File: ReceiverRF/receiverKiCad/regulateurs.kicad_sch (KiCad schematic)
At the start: 15 parts, among them SW5 SW_SPST, U2 NCV5501DT33RKG, U3 NJM2882F05-TE1

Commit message: changement vers footprint 1206
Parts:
- PWR_C2, PWR_C3: footprint Capacitor_SMD:C_0603_1608Metric -> Capacitor_SMD:C_1206_3216Metric
- PWR_C4, PWR_C5: footprint Capacitor_SMD:C_0402_1005Metric -> Capacitor_SMD:C_1206_3216Metric
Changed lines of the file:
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@@
 			)
 		)
-		(property "Footprint" "Capacitor_SMD:C_0603_1608Metric"
+		(property "Footprint" "Capacitor_SMD:C_1206_3216Metric"
 			(at 202.8952 90.17 0)
 			(effects
@@
 			)
 		)
-		(property "Footprint" "Capacitor_SMD:C_0603_1608Metric"
+		(property "Footprint" "Capacitor_SMD:C_1206_3216Metric"
 			(at 64.4652 77.47 0)
 			(effects
@@
 			)
 		)
-		(property "Footprint" "Capacitor_SMD:C_0402_1005Metric"
+		(property "Footprint" "Capacitor_SMD:C_1206_3216Metric"
 			(at 191.4652 100.33 0)
 			(effects
@@
 			)
 		)
-		(property "Footprint" "Capacitor_SMD:C_0402_1005Metric"
+		(property "Footprint" "Capacitor_SMD:C_1206_3216Metric"
 			(at 121.6152 97.79 0)
 			(effects

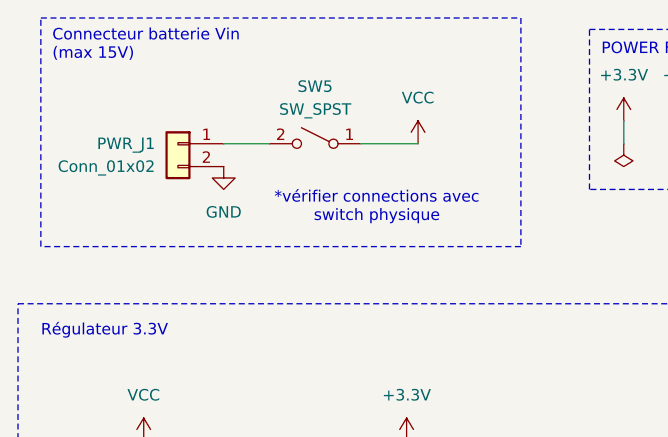
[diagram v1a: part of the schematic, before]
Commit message: changement BOM et choix nouvelles pièces 1206
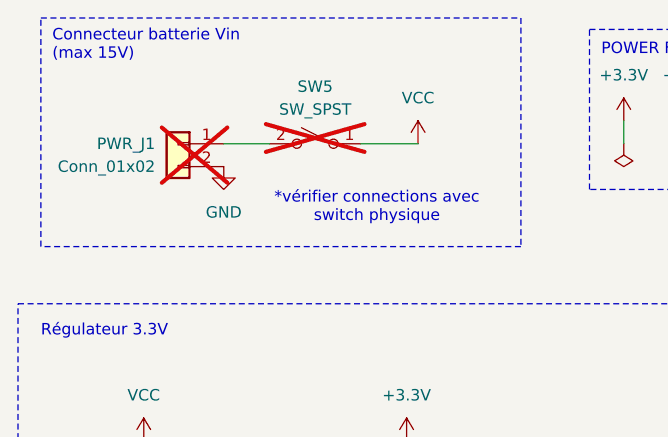
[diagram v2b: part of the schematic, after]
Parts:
- PWR_C2: Digikey 4713-GMC10X7R475K10NTCT-ND -> 1276-3182-1-ND
- PWR_C3: Digikey 2679-AGC0603X7R250-105KXPTR-ND -> 1276-1068-1-ND
- PWR_C4: Digikey 2679-AGC0402X7R500-104KNPTR-ND -> 399-C1206C104K5RACTUCT-ND
- PWR_C5: Digikey 2679-AGC0402X7R500-103KNPTR-ND -> 311-1174-1-ND
- PWR_J1, SW5: now not fitted
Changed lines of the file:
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@@
 			)
 		)
-		(property "Digikey" "  2679-AGC0603X7R250-105KXPTR-ND"
+		(property "Digikey" "1276-1068-1-ND"
 			(at 201.93 86.36 0)
 			(effects
@@
 		(in_bom yes)
 		(on_board yes)
-		(dnp no)
+		(dnp yes)
 		(property "Reference" "SW5"
 			(at 53.34 26.67 0)
@@
 			)
 		)
-		(property "Digikey" "4713-GMC10X7R475K10NTCT-ND"
+		(property "Digikey" "1276-3182-1-ND"
 			(at 63.5 73.66 0)
 			(effects
@@
 			)
 		)
-		(property "Digikey" "  2679-AGC0402X7R500-103KNPTR-ND"
+		(property "Digikey" "311-1174-1-ND"
 			(at 190.5 96.52 0)
 			(effects
@@
 		(in_bom yes)
 		(on_board yes)
-		(dnp no)
+		(dnp yes)
 		(property "Reference" "PWR_J1"
 			(at 35.56 33.02 0)
@@
 			)
 		)
-		(property "Digikey" "2679-AGC0402X7R500-104KNPTR-ND"
+		(property "Digikey" "399-C1206C104K5RACTUCT-ND"
 			(at 120.65 93.98 0)
 			(effects

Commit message: ideFIX v2 fix schematic, layout
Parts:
- removed SW5: SW_SPST, Footprints:SW_1MS02Q_CNK, symbol Switch:SW_SPST
- added D1: BZV55C18, Diode_SMD:D_MiniMELF, symbol Diode:BZV55C18
- added PWR_R5: 100k, Resistor_SMD:R_1206_3216Metric, symbol Device:R
- added Q2: PMOS, Footprints:SOT-23, symbol Simulation_SPICE:PMOS
- added SW5: SW_SPDT, Footprints:CS12ANW03_NKK, symbol Switch:SW_SPDT
- PWR_J1: footprint Connector_PinHeader_2.00mm:PinHeader_1x02_P2.00mm_Vertical -> Connector_PinHeader_2.54mm:PinHeader_1x02_P2.54mm_Vertical; now fitted
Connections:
- net GND: now also PWR_R5.2
- net VCC: now also D1.1 (K), Q2.3 (S)
- net at PWR_J1.1 (Pin_1): now also SW5.2 (B)
- new net: D1.2 (A), PWR_R5.1, Q2.2 (G)
- new net: Q2.1 (D), SW5.1 (A)
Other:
- note added: "Connecteur batterie Vin (max 20V)"
- note added: "Protection polarité inverse"
- note removed: "Connecteur batterie Vin (max 15V)"
- moved on the sheet: PWR_C1, PWR_C2, PWR_C3, PWR_C4, PWR_C5, PWR_D1, PWR_D2, PWR_R1, PWR_R2, PWR_R3, PWR_R4, U2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

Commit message: revision schematic before tracing
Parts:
- D1: value BZV55C18 -> SZMMSZ4679T1G
- PWR_R5: Digikey (none) -> 541-100KUTR-ND
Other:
- company: (none) -> GAUL
- title: (none) -> IdeFIX
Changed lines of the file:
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@@
 	(generator_version "8.0")
 	(paper "A4")
+	(title_block
+		(title "IdeFIX")
+		(rev "v2")
+		(company "GAUL")
+	)
 	(junction
 		(at 71.12 45.72)
@@
 			)
 		)
-		(property "Value" "BZV55C18"
+		(property "Value" "SZMMSZ4679T1G"
 			(at 81.28 41.9099 90)
 			(effects
@@
 			)
 		)
-		(property "Datasheet" "https://assets.nexperia.com/documents/data-sheet/BZV55_SER.pdf"
+		(property "Datasheet" "https://www.digikey.ca/en/products/detail/onsemi/SZMMSZ4679T1G/5404986?s=N4IgTCBcDaIMoC0CyTEBYBsB2AnAFQEYBxAeTgGE8BaAOQBEQBdAXyA"
 			(at 78.74 40.64 0)
 			(effects
@@
 			)
 		)
-		(property "Datasheet" "https://ngspice.sourceforge.io/docs/ngspice-html-manual/manual.xhtml#cha_MOSFETs"
+		(property "Datasheet" "https://www.digikey.ca/en/products/detail/onsemi/NTR4101PT1G/687096?s=N4IgTCBcDaIHIBUBKAWAjABjQBQWg4gPIDKAwggLRwAiIAugL5A"
 			(at 83.82 38.1 0)
 			(effects
@@
 			)
 		)
-		(property "Datasheet" "~"
+		(property "Datasheet" "https://www.digikey.ca/en/products/detail/vishay-dale/CRCW1206100KFKEAHP/2222454"
 			(at 71.12 50.8 0)
 			(effects
@@
 			)
 		)
-		(property "Digikey" ""
+		(property "Digikey" "  541-100KUTR-ND"
 			(at 71.12 50.8 0)
 			(effects

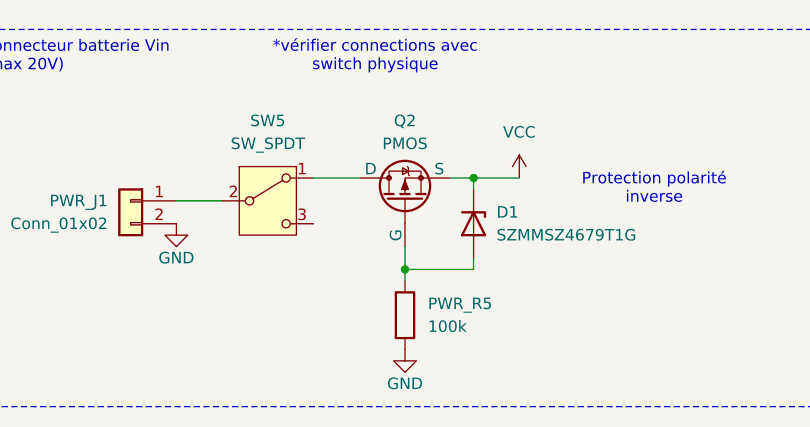
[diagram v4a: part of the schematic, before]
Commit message: finished silkscreen and added logos
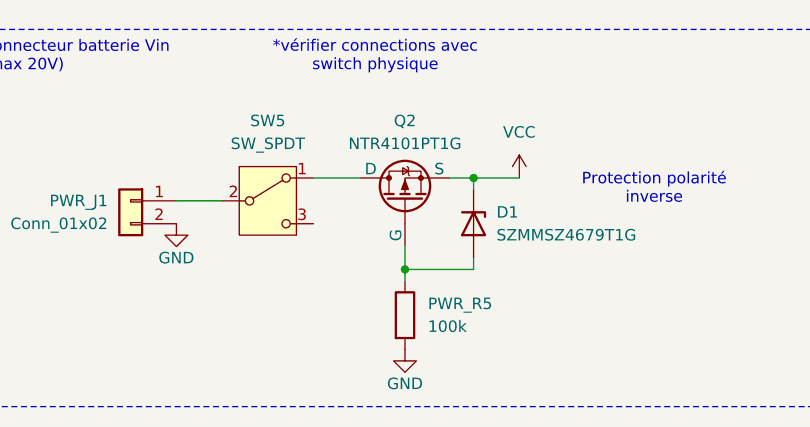
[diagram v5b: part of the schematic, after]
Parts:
- Q2: value PMOS -> NTR4101PT1G
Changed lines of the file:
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@@
 			)
 		)
-		(property "Value" "PMOS"
+		(property "Value" "NTR4101PT1G"
 			(at 71.12 31.75 90)
 			(effects

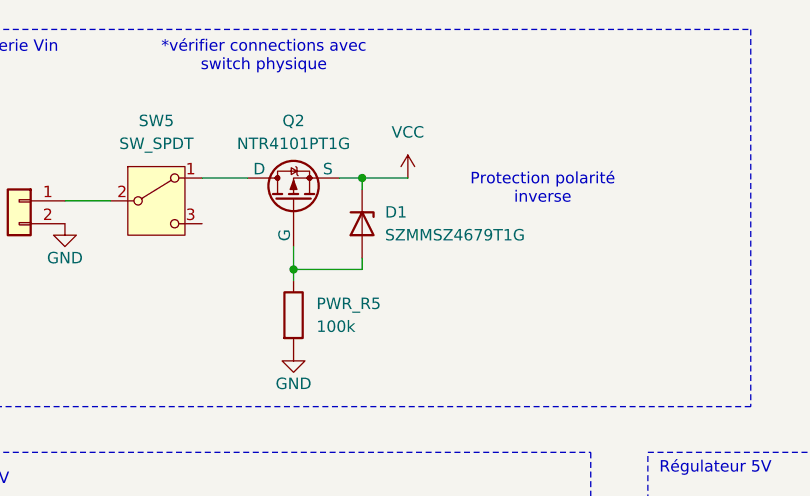
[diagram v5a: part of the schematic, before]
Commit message: fix zener diode footprint, thermal relief on SMA conn, more work on silkscreen
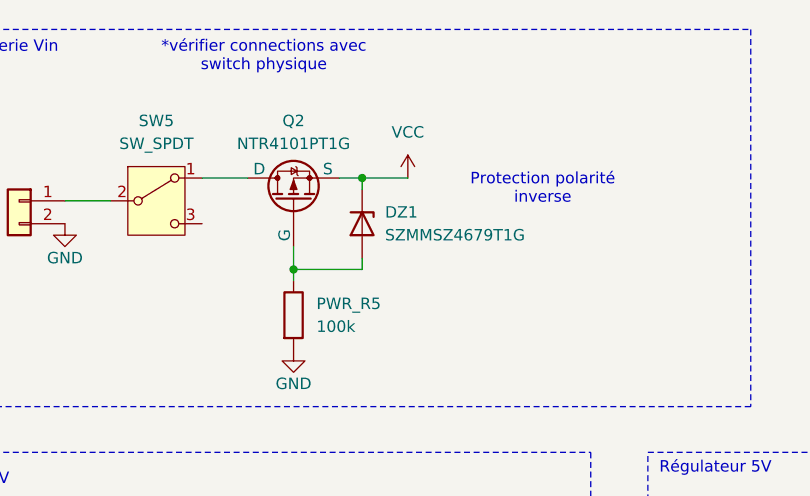
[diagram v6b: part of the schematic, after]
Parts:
- DZ1: renamed from D1; footprint Diode_SMD:D_MiniMELF -> Diode_SMD:D_SOD-123
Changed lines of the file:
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@@
 		(dnp no)
 		(fields_autoplaced yes)
-		(property "Reference" "D1"
+		(property "Reference" "DZ1"
 			(at 81.28 39.3699 90)
 			(effects
@@
 			)
 		)
-		(property "Footprint" "Diode_SMD:D_MiniMELF"
+		(property "Footprint" "Diode_SMD:D_SOD-123"
 			(at 74.295 40.64 0)
 			(effects
@@
 			(project ""
 				(path "/439ba515-58d4-4b14-87ab-b438dcf423a5/daa1b3d3-1e11-4b02-868f-dd095818f20a"
-					(reference "D1")
+					(reference "DZ1")
 					(unit 1)
 				)

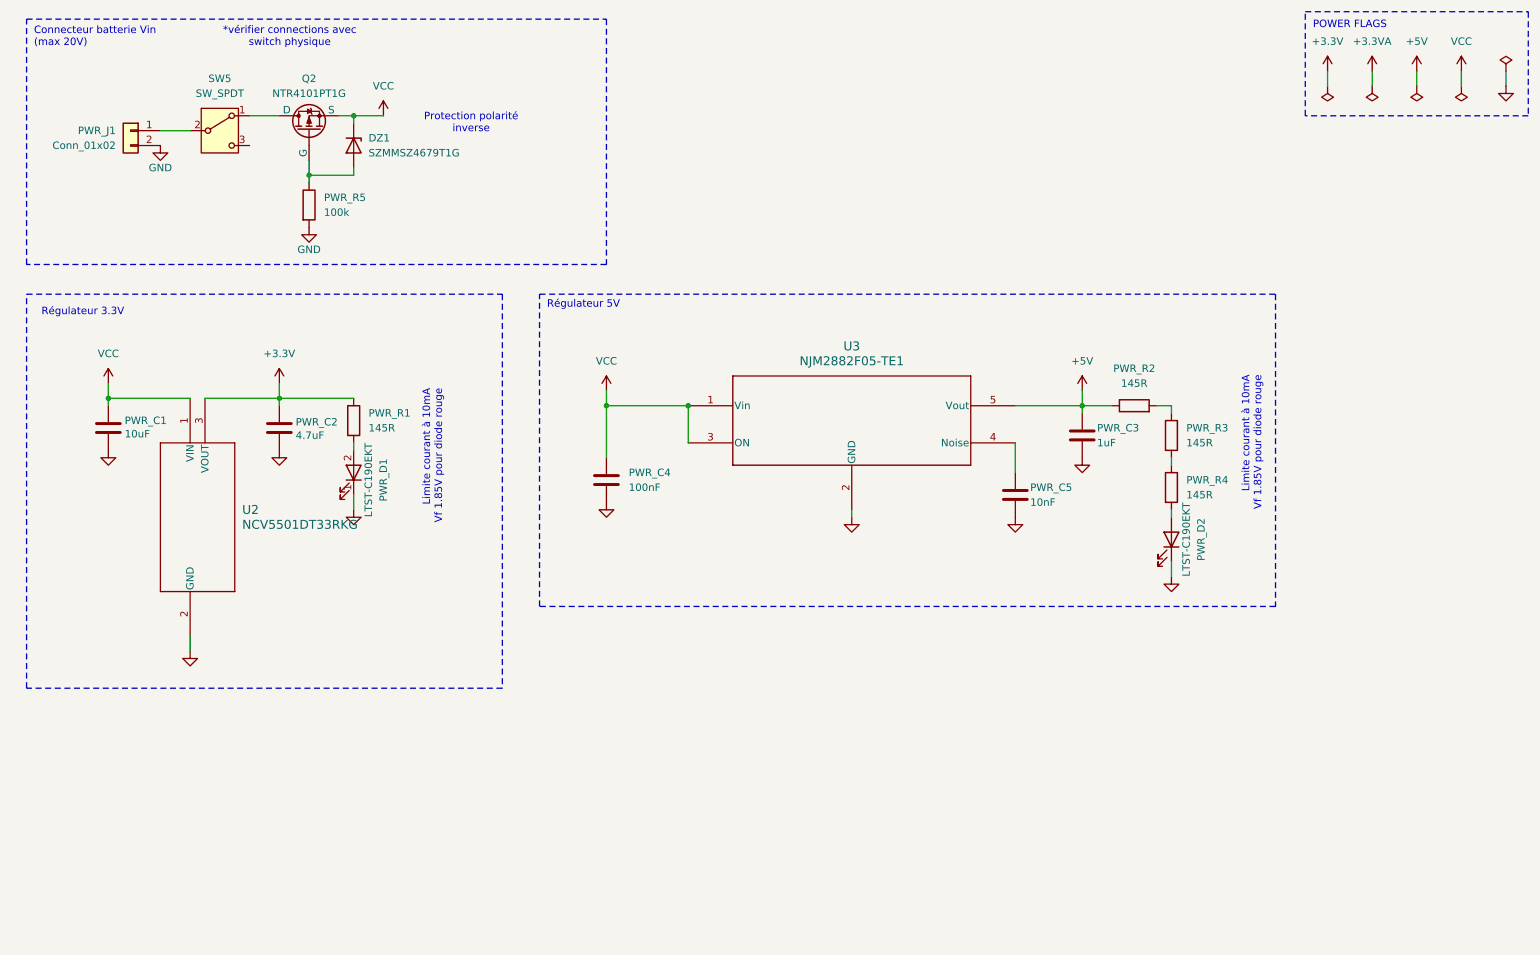
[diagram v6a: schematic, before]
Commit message: 3.2mm holes, XT30 connector, add polyfuse, minor fixes
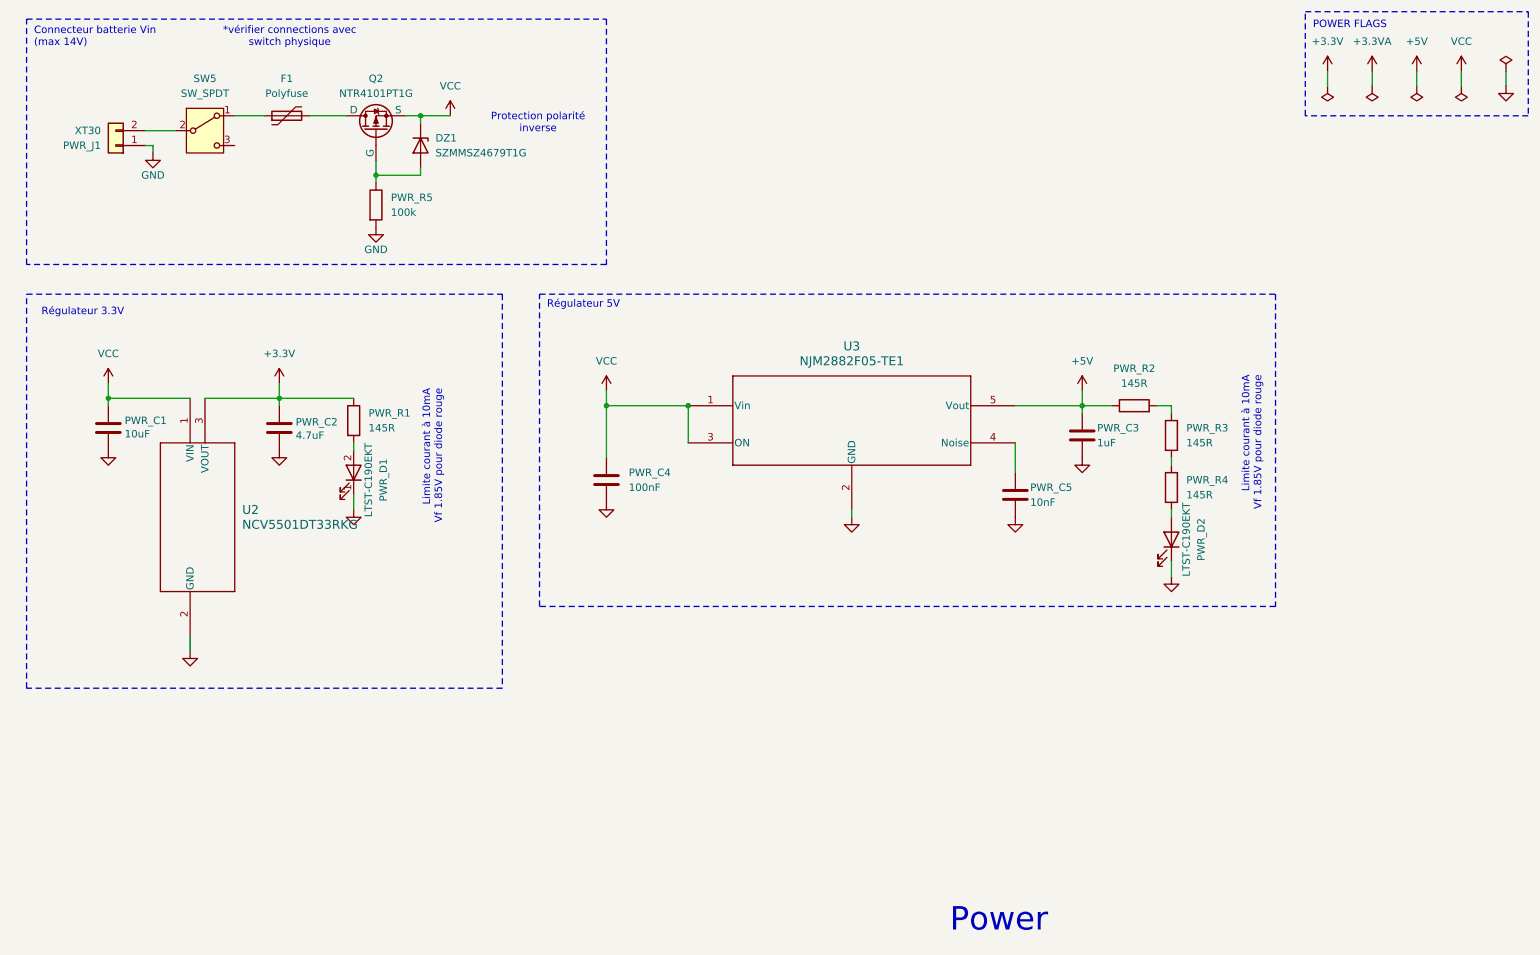
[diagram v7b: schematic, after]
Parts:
- added F1: Polyfuse, Footprints:Polyfuse, symbol Device:Polyfuse
- PWR_J1: value Conn_01x02 -> XT30; footprint Connector_PinHeader_2.54mm:PinHeader_1x02_P2.54mm_Vertical -> Connector_AMASS:AMASS_XT30U-M_1x02_P5.0mm_Vertical; Digikey (none) -> 1568-10474-ND
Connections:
- net GND: now also PWR_J1.1 (Pin_1); no longer PWR_J1.2 (Pin_2)
- net at SW5.1 (A): now also F1.1; no longer Q2.1 (D)
- net at SW5.2 (B): now also PWR_J1.2 (Pin_2); no longer PWR_J1.1 (Pin_1)
- new net: F1.2, Q2.1 (D)
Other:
- note added: "Connecteur batterie Vin (max 14V)"
- note added: "Power"
- note removed: "Connecteur batterie Vin (max 20V)"
- moved on the sheet: DZ1, PWR_J1, PWR_R5, Q2, SW5

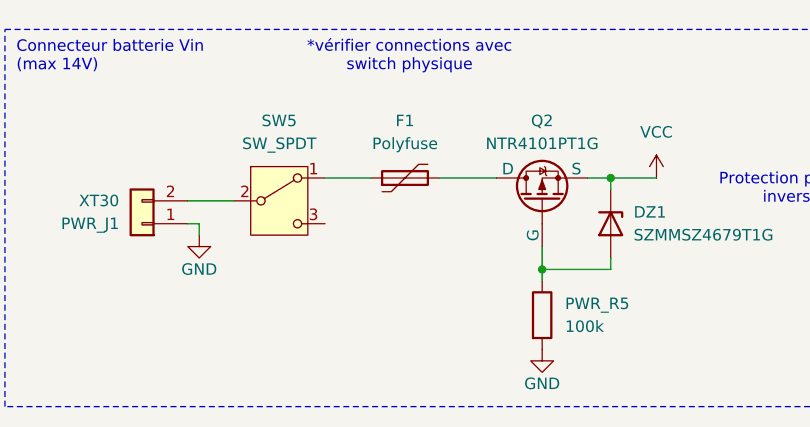
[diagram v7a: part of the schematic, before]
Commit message: Refactor timer handling and add TRANSMIT/RECEIVE definition macros
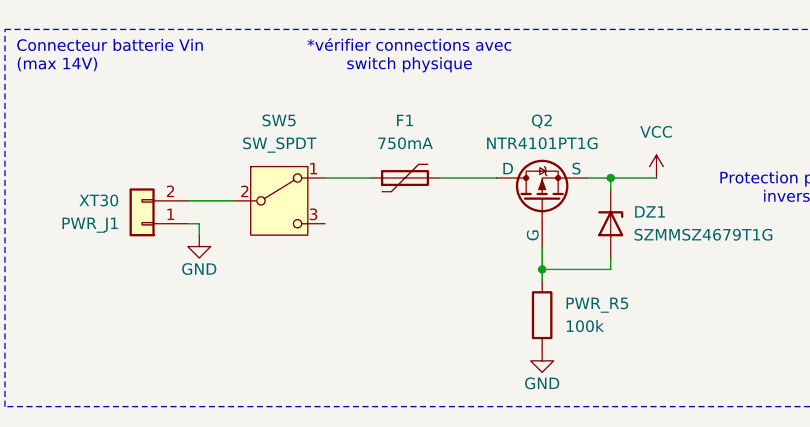
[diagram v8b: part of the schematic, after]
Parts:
- F1: value Polyfuse -> 750mA; Digikey 118-MF-NSMF075/13X-2TR-ND -> 118-MF-NSMF075/13X-2CT-ND
- PWR_C1: Digikey 2679-AGC1206X6S250-106KXETR-ND -> 1276-1804-1-ND
- PWR_D1, PWR_D2: Digikey 160-1182-1-ND -> 516-1422-1-ND
- PWR_R5: Digikey 541-100KUTR-ND -> 541-100KUCT-ND
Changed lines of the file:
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@@
 			)
 		)
-		(property "Description" ""
+		(property "Description" "145o Res"
 			(at 78.74 87.63 0)
 			(effects
@@
 			)
 		)
-		(property "Value" "Polyfuse"
+		(property "Value" "750mA"
 			(at 67.31 31.75 90)
 			(effects
@@
 			)
 		)
-		(property "Description" "MF-NSMF075/13X-2"
+		(property "Description" "Polyfuse"
 			(at 67.31 35.56 0)
 			(effects
@@
 			)
 		)
-		(property "Digikey" "  118-MF-NSMF075/13X-2TR-ND"
+		(property "Digikey" "118-MF-NSMF075/13X-2CT-ND"
 			(at 67.31 35.56 90)
 			(effects
@@
 			)
 		)
-		(property "Description" ""
+		(property "Description" "145o Res"
 			(at 218.44 99.06 0)
 			(effects
@@
 			)
 		)
-		(property "Description" ""
+		(property "Description" "1uF Cap"
 			(at 203.2 90.17 0)
 			(effects
@@
 			)
 		)
-		(property "Description" ""
+		(property "Description" "145o Res"
 			(at 212.09 85.09 0)
 			(effects
@@
 			)
 		)
-		(property "Description" "18V, 500mW, 5%, Zener diode, MiniMELF"
+		(property "Description" "2V zener diode"
 			(at 90.17 40.64 0)
 			(effects
@@
 			)
 		)
-		(property "Description" ""
+		(property "Description" "LDO 5V"
 			(at 135.89 85.09 0)
 			(effects
@@
 			)
 		)
-		(property "Description" ""
+		(property "Description" "4.7uF Cap"
 			(at 66.04 88.9 0)
 			(effects
@@
 			)
 		)
-		(property "Description" "P-MOSFET transistor, drain/source/gate"
+		(property "Description" "P-MOSFET transistor"
 			(at 82.55 38.1 0)
 			(effects
@@
 			)
 		)
-		(property "Description" ""
+		(property "Description" "10nF Cap"
 			(at 191.77 100.33 0)
 			(effects
@@
 			)
 		)
-		(property "Description" ""
+		(property "Description" "XT30 connector"
 			(at 38.1 40.64 0)
 			(effects
@@
 			)
 		)
-		(property "Description" ""
+		(property "Description" "100nF Cap"
 			(at 121.92 97.79 0)
 			(effects
@@
 			)
 		)
-		(property "Description" ""
+		(property "Description" "100k Res"
 			(at 82.55 50.8 0)
 			(effects
@@
 			)
 		)
-		(property "Digikey" "  541-100KUTR-ND"
+		(property "Digikey" "541-100KUCT-ND"
 			(at 82.55 50.8 0)
 			(effects
@@
 			)
 		)
-		(property "Description" ""
+		(property "Description" "145o Res"
 			(at 218.44 90.17 0)
 			(effects
@@
 			)
 		)
-		(property "Datasheet" "https://www.digikey.ca/en/products/detail/liteon/LTST-C190EKT/269229"
+		(property "Datasheet" "https://www.digikey.ca/en/products/detail/broadcom-limited/HSMS-C190/637746"
 			(at 78.74 96.52 0)
 			(effects
@@
 			)
 		)
-		(property "Description" ""
+		(property "Description" "Red led"
 			(at 78.74 96.52 0)
 			(effects
@@
 			)
 		)
-		(property "Digikey" "160-1182-1-ND"
+		(property "Digikey" "516-1422-1-ND"
 			(at 78.74 96.52 0)
 			(effects
@@
 			)
 		)
-		(property "Description" ""
+		(property "Description" "10uF Cap"
 			(at 36.83 88.9 0)
 			(effects
@@
 			)
 		)
-		(property "Digikey" "  2679-AGC1206X6S250-106KXETR-ND"
+		(property "Digikey" "1276-1804-1-ND"
 			(at 36.83 88.9 0)
 			(effects
@@
 			)
 		)
-		(property "Description" ""
+		(property "Description" "NPN BJT Transistor"
 			(at 50.8 124.46 0)
 			(effects
@@
 			)
 		)
-		(property "Datasheet" "https://www.digikey.ca/en/products/detail/liteon/LTST-C190EKT/269229"
+		(property "Datasheet" "https://www.digikey.ca/en/products/detail/broadcom-limited/HSMS-C190/637746"
 			(at 218.44 107.95 0)
 			(effects
@@
 			)
 		)
-		(property "Description" ""
+		(property "Description" "Red led"
 			(at 218.44 107.95 0)
 			(effects
@@
 			)
 		)
-		(property "Digikey" "160-1182-1-ND"
+		(property "Digikey" "516-1422-1-ND"
 			(at 218.44 107.95 0)
 			(effects
